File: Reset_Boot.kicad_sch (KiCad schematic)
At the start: 23 parts, among them J303 Micro_SD_Card, J304 Speaker, Q303 BSS138, SW301 KMR2, SW302 KMR2, U301 SSM2518CPZ

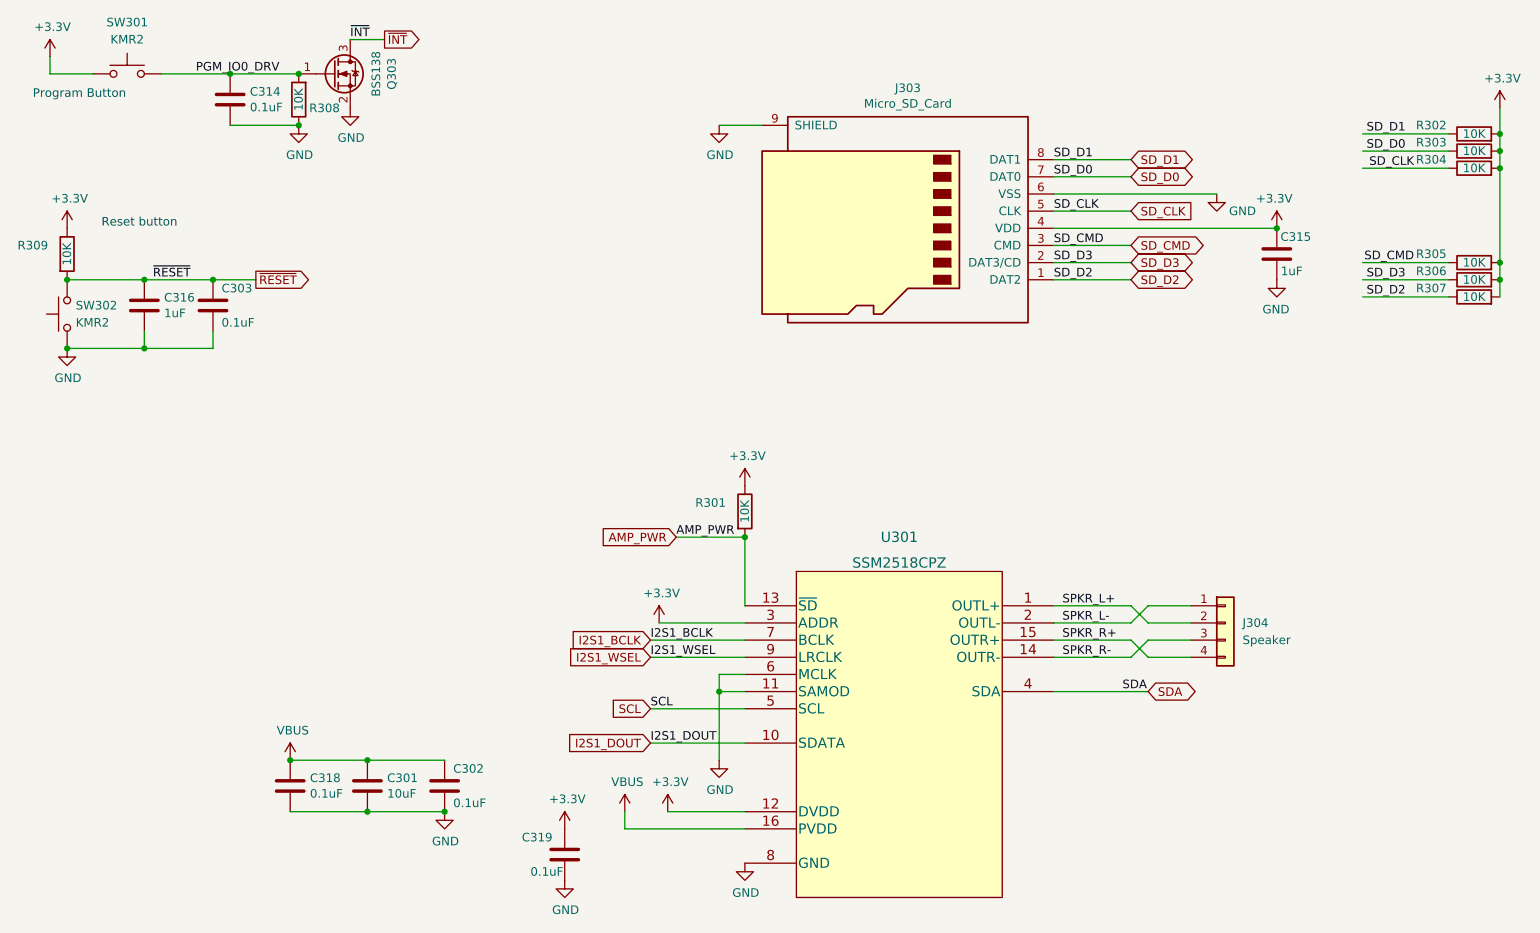
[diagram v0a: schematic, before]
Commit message: More updates
- Changed obsolete unidirectional level shifter to open-collector level shifter
- Replaced BSS138 level shifters with dedicated level shifter
- Changed all 5V I/O pins to have 33 ohm resistor in series
- Changed a few capacitors
- Cleanup tracks, vias, silkscreen, etc.

Signed-off-by: Aaron Williams <aaron.w2@gmail.com>
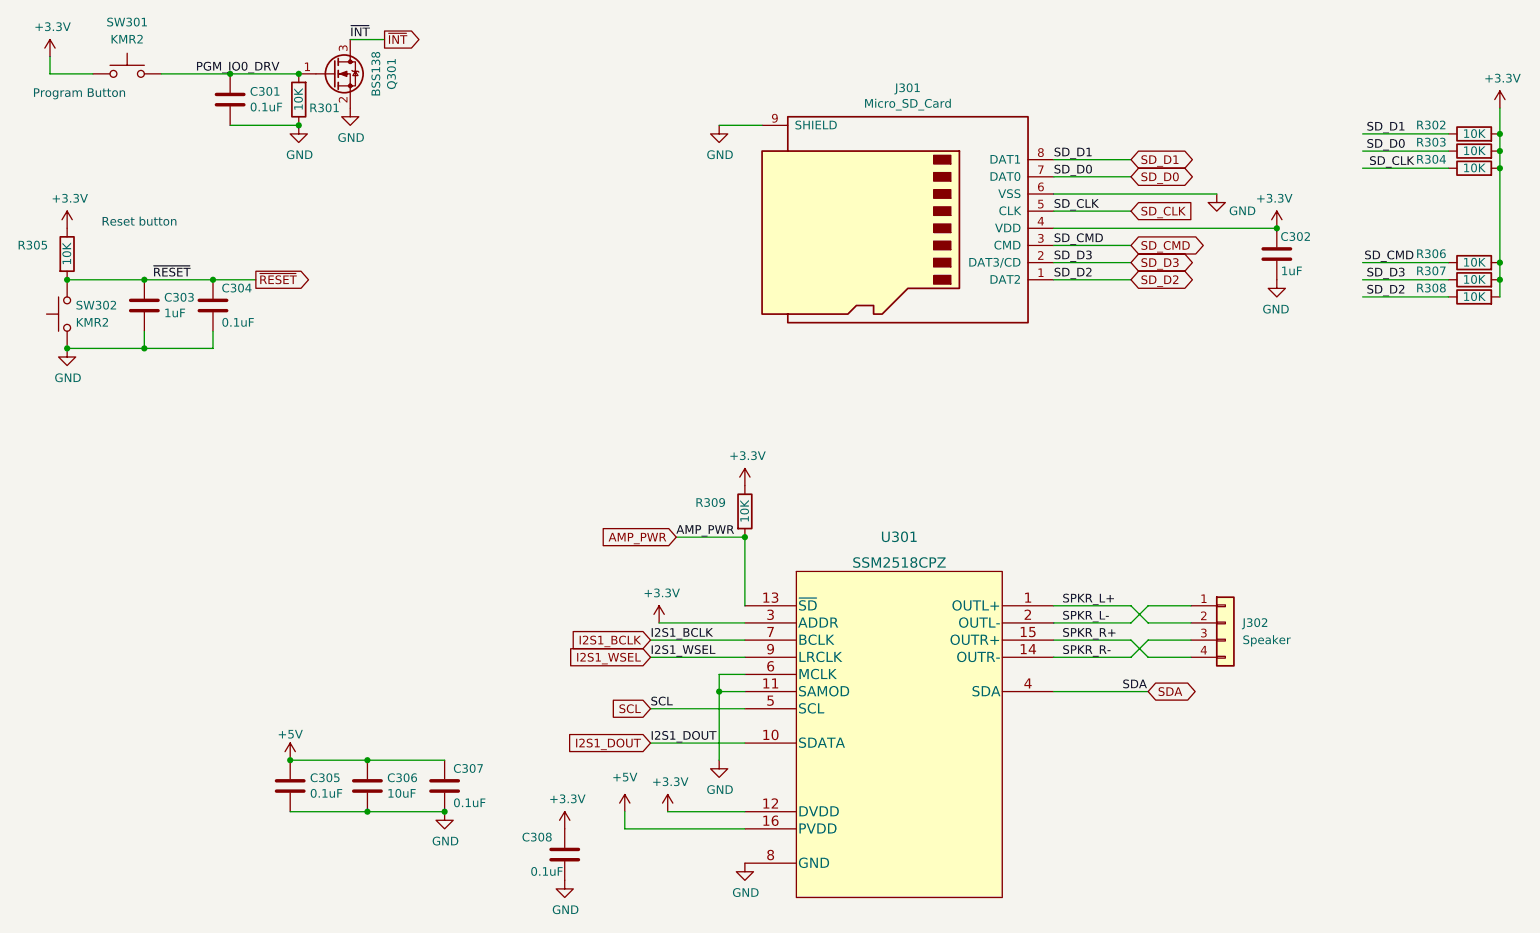
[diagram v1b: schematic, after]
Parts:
- Q301: renamed from Q303; footprint Package_TO_SOT_SMD:SOT-23 -> Package_TO_SOT_SMD:SOT-323_SC-70
- renumbered C314 to C301, C315 to C302, C316 to C303, C303 to C304, C318 to C305, C301 to C306, C302 to C307, C319 to C308, J303 to J301, J304 to J302, R308 to R301, R309 to R305, R305 to R306, R306 to R307, R307 to R308, R301 to R309
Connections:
- net PVDD renamed +5V

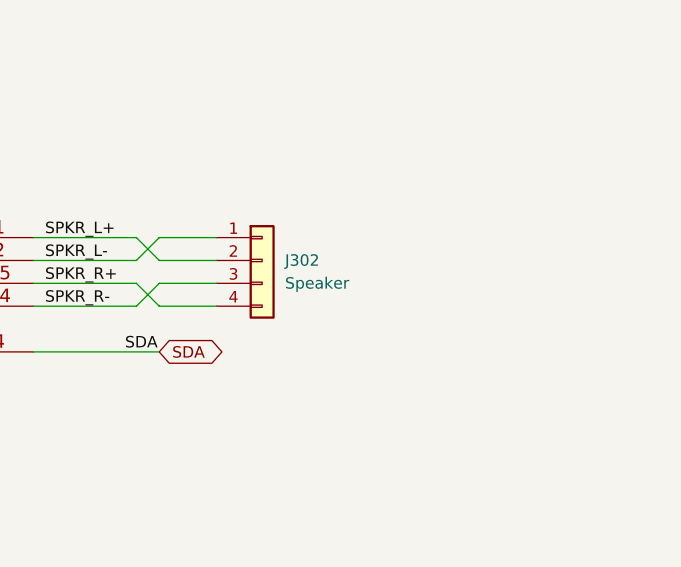
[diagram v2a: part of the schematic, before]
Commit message: More updates
- Removed 5V switch
- Added manual reset control of BNO085 to support booting remotely
- More minor cleanups
- Added jpeg renderings

Signed-off-by: Aaron Williams <aaron.w2@gmail.com>
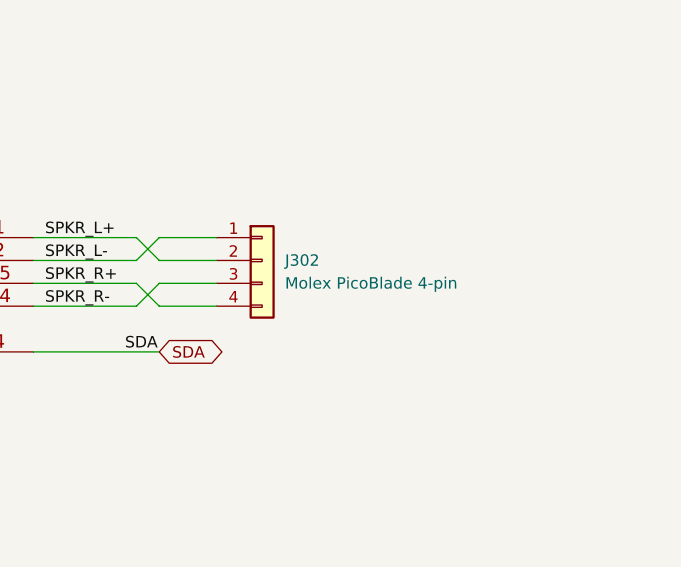
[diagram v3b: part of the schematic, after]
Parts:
- J301: DESC CONN MICRO SD CARD HINGED TYPE -> CONN MICRO SD CARD PUSH-PULL R/A; MFR Wuerth -> Molex; MPN 693072010801 -> 0475710001; SPN 732-3820-1-ND -> WM9731CT-ND; SPURL https://www.digikey.com/product-detail/en/w-rth-elektronik/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 -> https://www.digikey.com/en/products/detail/molex/0475710001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
- J302: value Speaker -> Molex PicoBlade 4-pin
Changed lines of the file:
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@@
       (effects (font (size 1.27 1.27)) (justify left))
     )
-    (property "Value" "Speaker" (id 1) (at 210.82 124.4599 0)
+    (property "Value" "Molex PicoBlade 4-pin" (id 1) (at 210.82 124.4599 0)
       (effects (font (size 1.27 1.27)) (justify left))
     )
@@
       (effects (font (size 1.27 1.27)) hide)
     )
-    (property "Datasheet" "" (id 3) (at 160.02 63.5 0)
-      (effects (font (size 1.27 1.27)) hide)
-    )
-    (property "MFR" "Wuerth" (id 4) (at 200.66 -107.95 0)
-      (effects (font (size 1.27 1.27)) hide)
-    )
-    (property "MPN" "693072010801" (id 5) (at 200.66 -107.95 0)
+    (property "Datasheet" "https://media.digikey.com/pdf/Data%20Sheets/Molex%20PDFs/0475710001_Elect_Model.pdf" (id 3) (at 160.02 63.5 0)
+      (effects (font (size 1.27 1.27)) hide)
+    )
+    (property "MFR" "Molex" (id 4) (at 200.66 -107.95 0)
+      (effects (font (size 1.27 1.27)) hide)
+    )
+    (property "MPN" "0475710001" (id 5) (at 200.66 -107.95 0)
       (effects (font (size 1.27 1.27)) hide)
     )
@@
       (effects (font (size 1.27 1.27)) hide)
     )
-    (property "SPN" "732-3820-1-ND" (id 7) (at 200.66 -107.95 0)
-      (effects (font (size 1.27 1.27)) hide)
-    )
-    (property "SPURL" "https://www.digikey.com/product-detail/en/w-rth-elektronik/693072010801/732-3820-1-ND/3124605" (id 8) (at 200.66 -107.95 0)
-      (effects (font (size 1.27 1.27)) hide)
-    )
-    (property "DESC" "CONN MICRO SD CARD HINGED TYPE" (id 9) (at 200.66 -81.28 0)
-      (effects (font (size 1.27 1.27)) hide)
-    )
+    (property "SPN" "WM9731CT-ND" (id 7) (at 200.66 -107.95 0)
+      (effects (font (size 1.27 1.27)) hide)
+    )
+    (property "SPURL" "https://www.digikey.com/en/products/detail/molex/0475710001/3262277" (id 8) (at 200.66 -107.95 0)
+      (effects (font (size 1.27 1.27)) hide)
+    )
+    (property "DESC" "CONN MICRO SD CARD PUSH-PULL R/A" (id 9) (at 200.66 -81.28 0)
+      (effects (font (size 1.27 1.27)) hide)
+    )
